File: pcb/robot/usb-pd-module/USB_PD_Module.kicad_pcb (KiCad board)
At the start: 4 copper layers, 77 x 13.5 mm, 57 parts, among them J4 USB4151-GF-C, J9 Conn_01x16, U11 MAX77958EWV+T, U15 TPD1E05U06, U16 fpf1048bucx, U17 TPS61253AYFFT, U19 TPD1E05U06, U20 TPD1E05U06, U21 TPD1E05U06, U22 TPD1E05U06, U23 TPD1E05U06, U24 TVS0500DRV

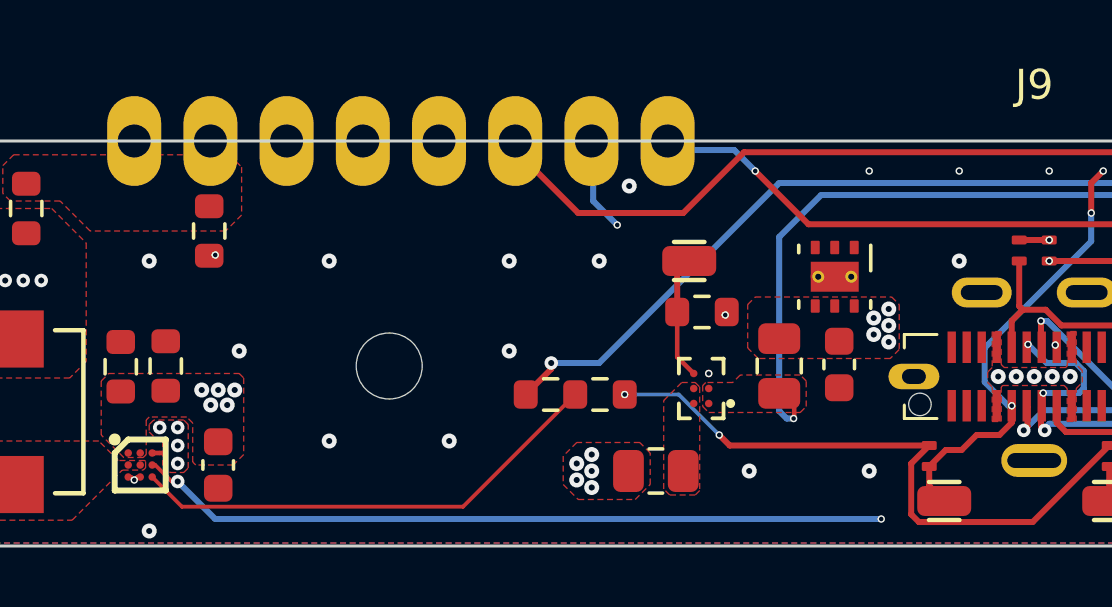
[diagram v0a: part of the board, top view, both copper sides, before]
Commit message: Added the TPS22950CDDCR
Generation, upgrade, and replacement of devices in BOM for manufacturing at JLCPCB.
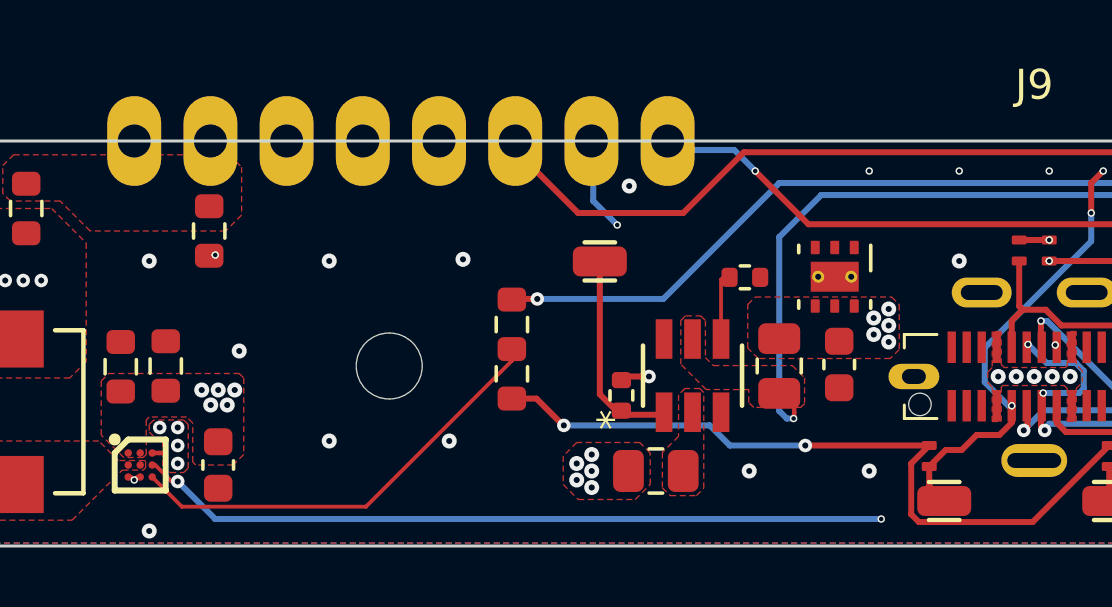
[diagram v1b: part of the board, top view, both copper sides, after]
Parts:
- removed R65: 10M, robot:R_0603_1608Metric
- removed U16: fpf1048bucx, robot:BGA6N50P3X2_146X96X62N
- added R1: 100, robot:R_0402_1005Metric, F.Cu at (117.7, 115.5)
- added R2: 422, robot:R_0402_1005Metric, F.Cu at (121.9, 111.5)
- added U1: TPS22950CDDCR, robot:DDC6_TEX, F.Cu at (120.1, 114.8)
- moved TP5 2.98 mm to (117.0, 111.0)
- moved R95 2.56 mm to (114.1, 114.0), turned to 90 degrees
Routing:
- net /AGND: track 71.6 -> 75.3 mm
- net Net-(U1-ON): track 4.14 -> 6.89 mm
- net Net-(U1-ILIM): track 0.00 -> 2.16 mm
- net Net-(U17-MODE): track 16.1 -> 14.8 mm
- net /GPIO4: track 32.4 -> 33.5 mm
- net /VIO2: track 45.1 -> 44.1 mm
- net GND: vias 55 -> 52
